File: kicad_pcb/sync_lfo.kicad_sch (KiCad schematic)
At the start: 23 parts, among them J1 CLOCK IN, J2 OUT, J3 Connector 2x8

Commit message: feat: :sparkles: rev 0.2 pcb and schematics
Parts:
- added R8: R 33K, Resistor_THT:R_Axial_DIN0204_L3.6mm_D1.6mm_P2.54mm_Vertical, symbol Device:R
- C1, C2, C3, C4: value C -> C 220pF; footprint Capacitor_THT:C_Disc_D3.0mm_W1.6mm_P2.50mm -> Capacitor_THT:C_Disc_D4.3mm_W1.9mm_P5.00mm
- C5: value C -> C 4.7 µF
- R1, R4, R5, R6, R7: value R -> R 470
- R2: value R -> R 1K
- R3: value R -> R 100K
- renumbered RV1-AMP to RV1-AMP1, RV2-PHASE to RV2-PHASE1, RV3-FORM to RV3-FORM1, RV4-MOD to RV4-MOD1
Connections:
- net +12V: now also J3.7 (Pin_7), J3.8 (Pin_8); no longer J3.10 (Pin_10), J3.9 (Pin_9)
- net GND: now also J3.10 (Pin_10), J3.11 (Pin_11), J3.12 (Pin_12), J3.13 (Pin_13), J3.14 (Pin_14), J3.9 (Pin_9); no longer J3.3 (Pin_3), J3.4 (Pin_4), J3.5 (Pin_5), J3.6 (Pin_6), J3.7 (Pin_7), J3.8 (Pin_8)
- net at A1.13 (D10), R7.1: now also R8.1; no longer D3.2 (A)
- new net: D3.2 (A), R8.2
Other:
- moved on the sheet: D3

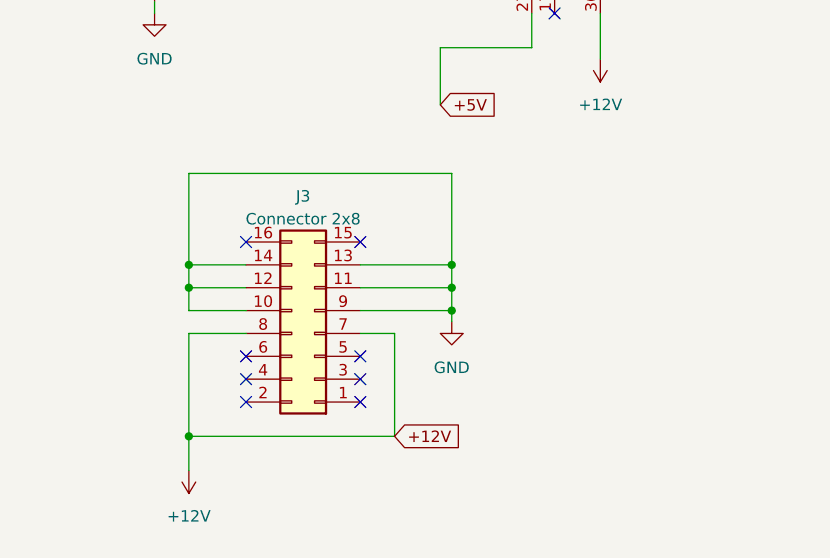
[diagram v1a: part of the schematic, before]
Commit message: feat: :sparkles: 10pin connector, drill holes, for distance, better routing
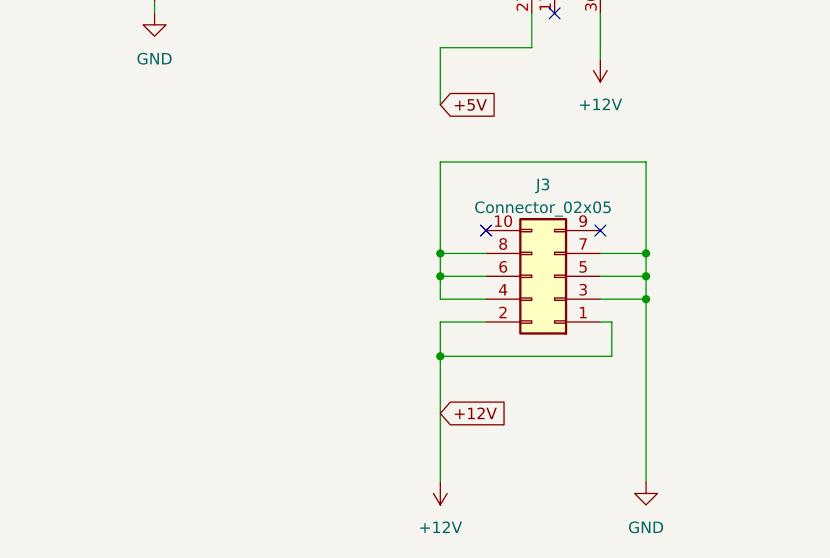
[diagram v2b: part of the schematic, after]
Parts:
- removed J3: Connector 2x8, Connector_IDC:IDC-Header_2x08_P2.54mm_Vertical, symbol Connector_Generic:Conn_02x08_Odd_Even
- added J3: Connector_02x05, Connector_IDC:IDC-Header_2x05_P2.54mm_Vertical, symbol Connector_Generic:Conn_02x05_Odd_Even
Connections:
- net +12V: now also J3.1 (Pin_1), J3.2 (Pin_2)
- net GND: now also J3.3 (Pin_3), J3.4 (Pin_4), J3.5 (Pin_5), J3.6 (Pin_6), J3.7 (Pin_7), J3.8 (Pin_8)
- no-connect marks 29 -> 23

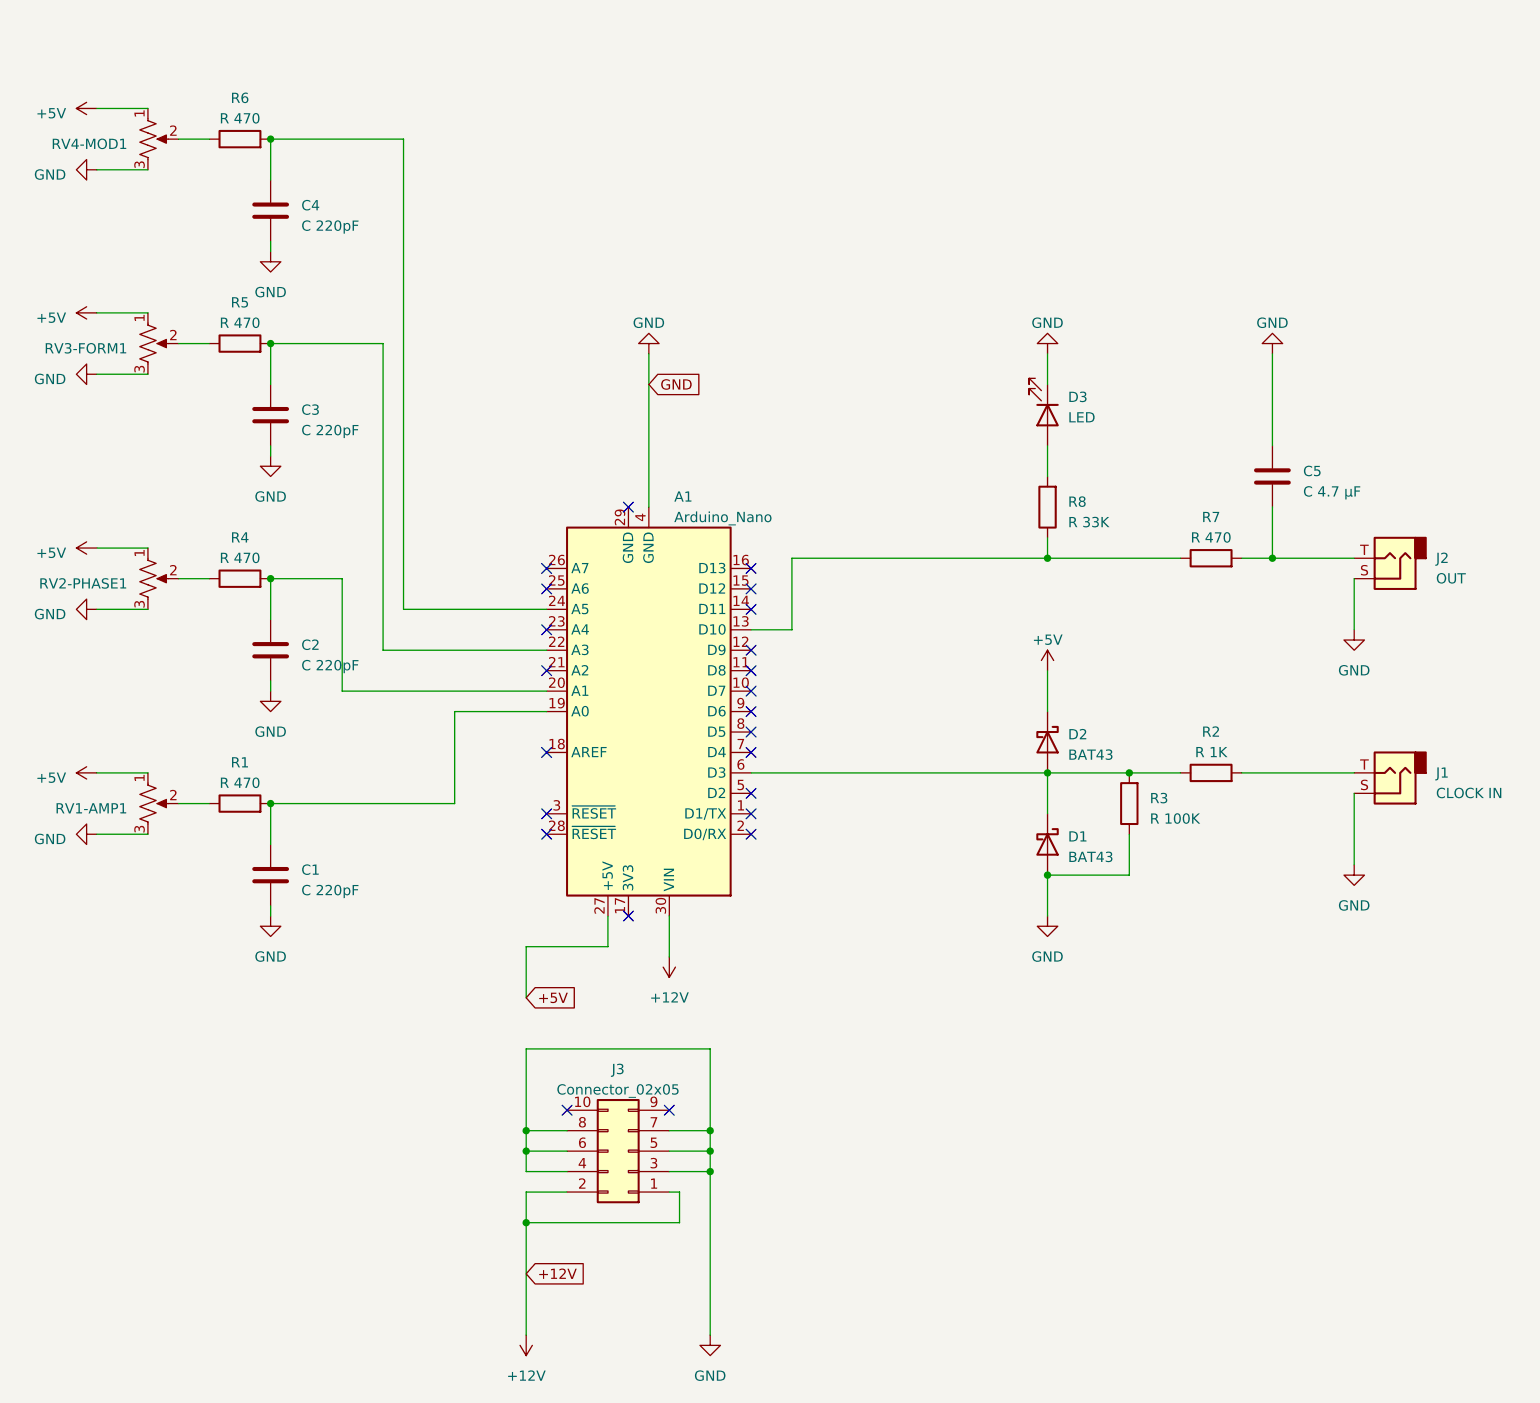
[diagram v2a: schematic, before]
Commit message: feat: :sparkles: inv output, new design, reposition
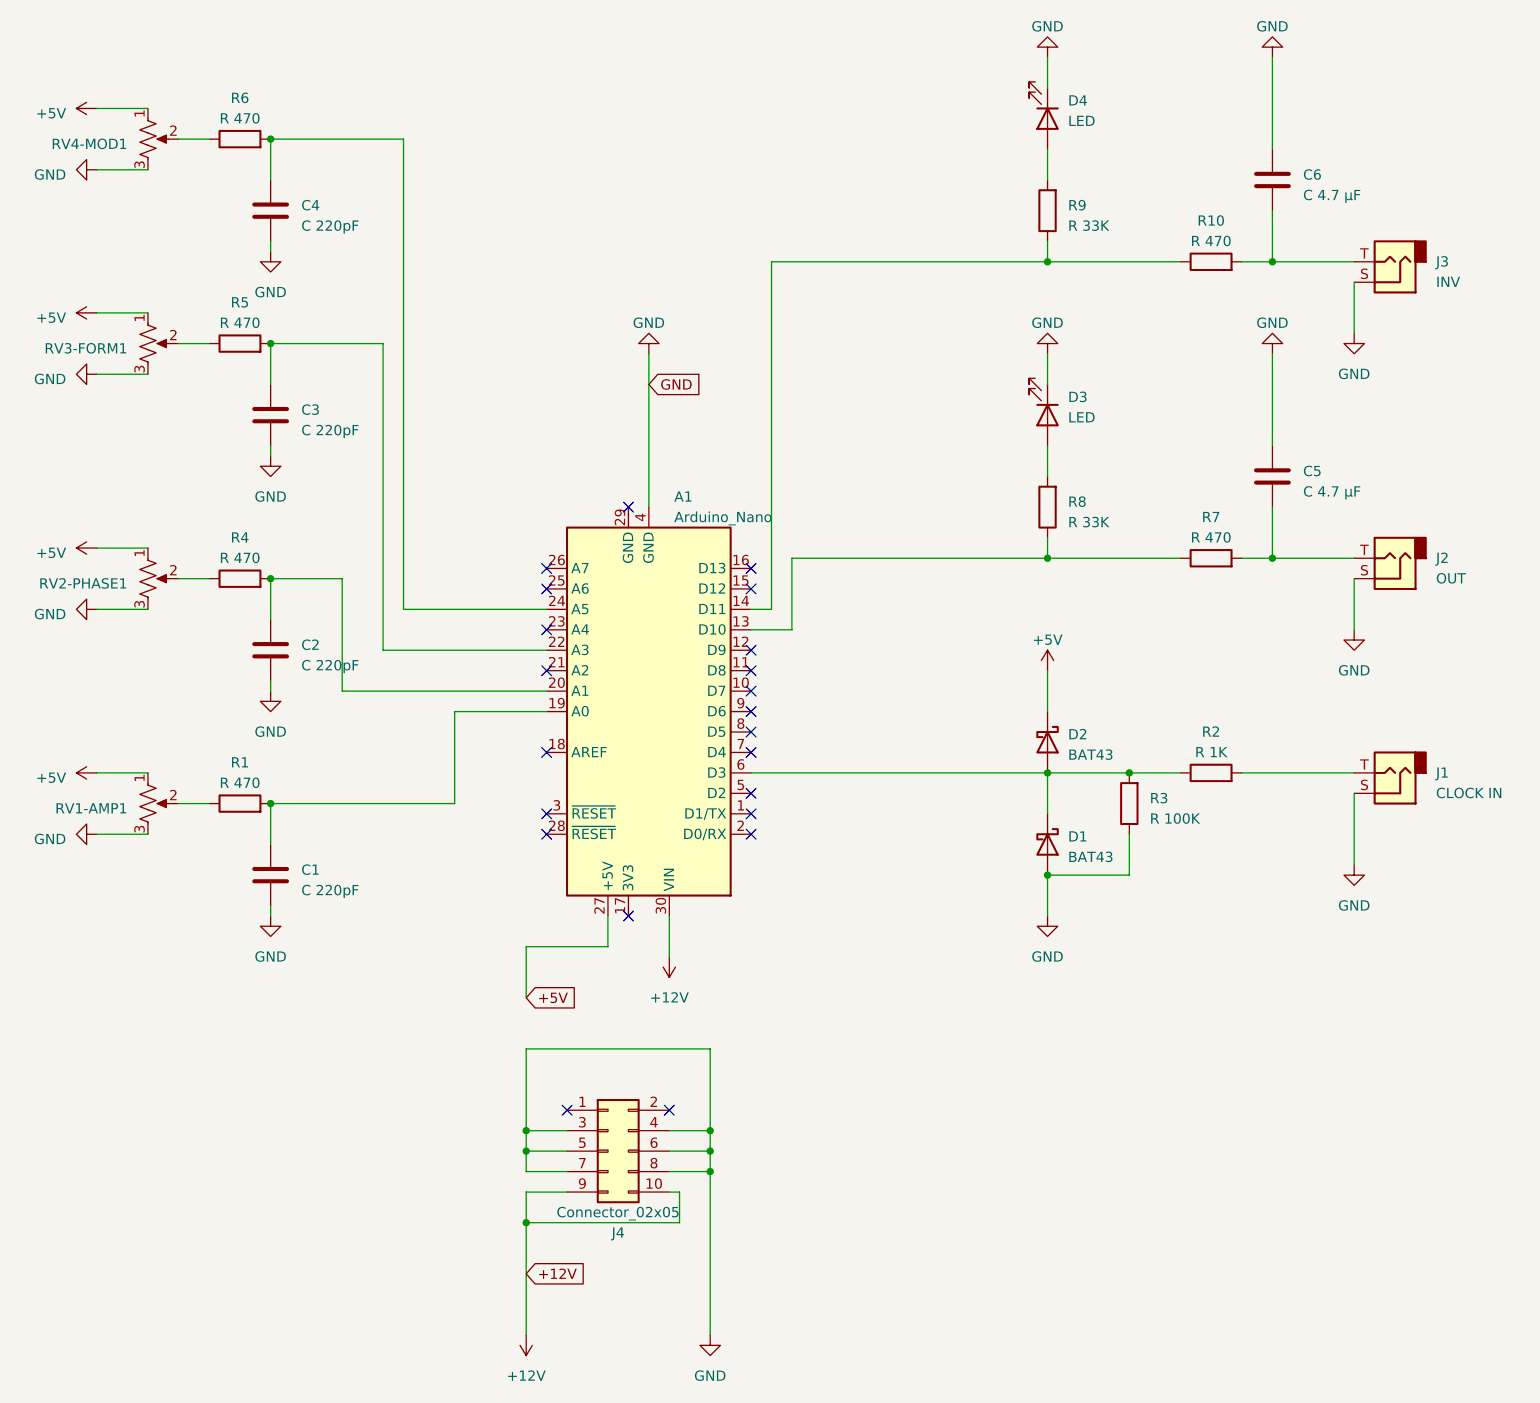
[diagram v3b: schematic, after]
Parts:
- added C6: C 4.7 µF, Capacitor_THT:C_Radial_D5.0mm_H11.0mm_P2.00mm, symbol Device:C
- added D4: LED, LED_THT:LED_D3.0mm, symbol Device:LED
- added J3: INV, Connector_Audio:Jack_3.5mm_QingPu_WQP-PJ398SM_Vertical_CircularHoles, symbol Connector_Audio:AudioJack2
- added R10: R 470, Resistor_THT:R_Axial_DIN0204_L3.6mm_D1.6mm_P2.54mm_Vertical, symbol Device:R
- added R9: R 33K, Resistor_THT:R_Axial_DIN0204_L3.6mm_D1.6mm_P2.54mm_Vertical, symbol Device:R
- renumbered J3 to J4
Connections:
- net +12V: now also J4.10 (Pin_10), J4.9 (Pin_9); no longer J4.1 (Pin_1), J4.2 (Pin_2)
- net GND: now also C6.1, D4.1 (K), J3.S
- net at A1.14 (D11): now also R10.1, R9.1
- new net: C6.2, J3.T, R10.2
- new net: D4.2 (A), R9.2
- no-connect marks 23 -> 22
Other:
- moved on the sheet: J4
